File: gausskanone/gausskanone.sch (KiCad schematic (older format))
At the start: 63 parts, among them J3 Power Input, J5 Speedsensor, Q1 Q_NMOS_DGS, Q2 Q_NMOS_DGS, Q3 Q_NMOS_DGS, SW1 SW_DPST, SW2 SW_DPST, U2 Si8220, U3 IE1212D, U5 IL300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

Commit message: Add files via upload
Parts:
- removed U?: LT1037, symbol Amplifier_Operational:OP249
- added R?: 16K, symbol Device:R
- added U? (x2): OPA1678, symbol Amplifier_Operational:OPA1678
- R6: value R -> 2K
- RV?: value R_POT -> 2K
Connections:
- wire segments 272 -> 273
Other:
- note added: "VOUT 6V\n\n"
- note added: "op versorgung +-12V\n"
- note removed: "VOUT\n"
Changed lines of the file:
@@
 P 10900 950
 F 0 "RV?" V 10693 950 50  0000 C CNN
-F 1 "R_POT" V 10784 950 50  0000 C CNN
+F 1 "2K" V 10784 950 50  0000 C CNN
 F 2 "" H 10900 950 50  0001 C CNN
 F 3 "~" H 10900 950 50  0001 C CNN
@@
 $EndComp
 Text Notes 15250 3550 0    50   ~ 0
-VOUT\n
+VOUT 6V\n\n
 Wire Wire Line
 	14400 3600 15300 3600
@@
 $EndComp
 $Comp
-L Amplifier_Operational:OP249 U?
-U 1 1 5DF6E34D
-P 12950 1150
-F 0 "U?" H 12950 1517 50  0000 C CNN
-F 1 "LT1037" H 12950 1426 50  0000 C CNN
-F 2 "" H 12950 1150 50  0001 C CNN
-F 3 "https://www.analog.com/media/en/technical-documentation/data-sheets/OP249.pdf" H 12950 1150 50  0001 C CNN
-	1    12950 1150
-	1    0    0    -1
-$EndComp
-$Comp
 L Connector:Conn_01x02_Female J?
 U 1 1 5E147FCA
@@
 Connection ~ 9400 1050
 Wire Wire Line
-	10100 950  10750 950
-Wire Wire Line
 	10100 1050 10100 950
 Wire Wire Line
@@
 P 11200 1250
 F 0 "R6" H 11270 1296 50  0000 L CNN
-F 1 "R" H 11270 1205 50  0000 L CNN
+F 1 "2K" H 11270 1205 50  0000 L CNN
 F 2 "" V 11130 1250 50  0001 C CNN
 F 3 "~" H 11200 1250 50  0001 C CNN
@@
 	1    0    0    -1
 $EndComp
+$Comp
+L Amplifier_Operational:OPA1678 U?
+U 1 1 5E25FF63
+P 12950 1150
+F 0 "U?" H 12950 1517 50  0000 C CNN
+F 1 "OPA1678" H 12950 1426 50  0000 C CNN
+F 2 "" H 12950 1150 50  0001 C CNN
+F 3 "http://www.ti.com/lit/ds/symlink/opa1678.pdf" H 12950 1150 50  0001 C CNN
+	1    12950 1150
+	1    0    0    -1
+$EndComp
+$Comp
+L Amplifier_Operational:OPA1678 U?
+U 3 1 5E280D7A
+P 15300 1300
+F 0 "U?" H 15258 1346 50  0000 L CNN
+F 1 "OPA1678" H 15258 1255 50  0000 L CNN
+F 2 "" H 15300 1300 50  0001 C CNN
+F 3 "http://www.ti.com/lit/ds/symlink/opa1678.pdf" H 15300 1300 50  0001 C CNN
+	3    15300 1300
+	1    0    0    -1
+$EndComp
+Text Notes 15000 950  0    50   ~ 0
+op versorgung +-12V\n
+$Comp
+L Device:R R?
+U 1 1 5E2B2007
+P 10400 950
+F 0 "R?" H 10470 996 50  0000 L CNN
+F 1 "16K" H 10470 905 50  0000 L CNN
+F 2 "" V 10330 950 50  0001 C CNN
+F 3 "~" H 10400 950 50  0001 C CNN
+	1    10400 950
+	0    1    1    0
+$EndComp
+Wire Wire Line
+	10100 950  10250 950
+Wire Wire Line
+	10550 950  10750 950
 $EndSCHEMATC

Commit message: PCB ready for order
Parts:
- removed C15: CP, symbol Device:CP
- removed Q1, Q2, Q3: Q_NMOS_DGS, symbol Device:Q_NMOS_DGS
- removed R?: 70K, symbol Device:R
- removed SW1, SW2: SW_DPST, symbol Switch:SW_DPST
- removed TP1: UC, symbol Connector:TestPoint
- removed U3: IE1212D, Project:IEXXXXD, symbol Regulator_Switching:CRE1S0305S3C
- removed U?: DA04-11SRWA, Display_7Segment:DA04-11SURKWA, symbol Display_Character:DA04-11SRWA
- added C1, C4: C, Capacitor_SMD:C_0805_2012Metric, symbol Device:C
- added J3: System Bus, Connector_PinHeader_2.54mm:PinHeader_1x02_P2.54mm_Vertical, symbol Connector:Conn_01x02_Female
- added Q1: Overvoltage, Package_TO_SOT_SMD:TO-252-3_TabPin2, symbol Device:Q_NMOS_GDS
- added Q2: CSD19536KTT, Package_TO_SOT_SMD:TO-263-3_TabPin2, symbol Device:Q_NMOS_GDS
- added Q3: DCDC, Package_TO_SOT_SMD:TO-252-3_TabPin2, symbol Device:Q_NMOS_GDS
- added R10: 47K, Resistor_SMD:R_0805_2012Metric, symbol Device:R
- added RV2: 10K, Potentiometer_THT:Potentiometer_Bourns_3339P_Vertical, symbol Device:R_POT
- added RV3: 20K, Potentiometer_THT:Potentiometer_Bourns_3339P_Vertical, symbol Device:R_POT
- added RV4: 2K, Potentiometer_THT:Potentiometer_Bourns_3339P_Vertical, symbol Device:R_POT
- added SW1, SW2: SW_DIP_x01, Button_Switch_THT:SW_PUSH_6mm_H7.3mm, symbol Switch:SW_DIP_x01
- added U2: DPU01, Project:DPU01, symbol Project:DPU01
- C10: renamed from C7; footprint (none) -> Capacitor_SMD:C_0805_2012Metric
- C11: renamed from C8; footprint (none) -> Capacitor_SMD:C_0805_2012Metric
- C12: renamed from C9; footprint (none) -> Capacitor_SMD:C_0805_2012Metric
- C13: renamed from C10; footprint (none) -> Capacitor_SMD:C_0805_2012Metric
- C14: renamed from C11; footprint (none) -> Capacitor_SMD:C_0805_2012Metric
- C15: renamed from C12; footprint (none) -> Capacitor_SMD:C_0805_2012Metric
- C16: renamed from C13; footprint (none) -> Capacitor_SMD:C_0805_2012Metric
- C17: renamed from C14; footprint (none) -> Capacitor_SMD:C_0805_2012Metric
- C2: footprint (none) -> Project:BC 58223
- C3: renamed from C?; footprint (none) -> Capacitor_SMD:C_0805_2012Metric
- C5: renamed from C16; footprint (none) -> Capacitor_SMD:C_0805_2012Metric
- C6: renamed from C4; footprint (none) -> Capacitor_THT:CP_Radial_D6.3mm_P2.50mm
- C8: renamed from C5; footprint (none) -> Capacitor_THT:CP_Radial_D8.0mm_P2.50mm
- C9: renamed from C6; footprint (none) -> Capacitor_SMD:C_0805_2012Metric
- D1: renamed from D2; value 63V -> D Overv; footprint (none) -> Diode_SMD:D_SOD-123
- D2: renamed from D3; value D -> Flyback; footprint (none) -> Diode_SMD:D_SOD-123F
- D3: renamed from D1; value D_Schottky -> D Sec; footprint (none) -> Diode_SMD:D_SOD-123F
- D4: renamed from D9; value D -> D Input; footprint (none) -> Diode_SMD:D_SOD-123F
- D5: renamed from D10; value LED -> Green; footprint (none) -> LED_SMD:LED_0805_2012Metric_Castellated
- D6: renamed from D11; value LED -> Red; footprint (none) -> LED_SMD:LED_0805_2012Metric_Castellated
- D7: value D_Schottky -> D Aux; footprint (none) -> Diode_SMD:D_SOD-123
- D8: footprint (none) -> Diode_SMD:D_SOD-123
- J1: renamed from J3; footprint (none) -> TerminalBlock_RND:TerminalBlock_RND_205-00289_1x04_P5.08mm_Horizontal
- J2: renamed from J5; footprint (none) -> Connector_PinHeader_2.54mm:PinHeader_1x04_P2.54mm_Vertical
- J4: renamed from J?; footprint (none) -> Connector_PinHeader_2.54mm:PinHeader_1x02_P2.54mm_Vertical
- JP1: footprint (none) -> Connector_PinHeader_2.54mm:PinHeader_1x02_P2.54mm_Vertical
- L1: renamed from L2; footprint (none) -> Project:GK-L01
- L2: renamed from L1; footprint (none) -> Project:PA582-AL
- R1: renamed from R?; value 16K -> R; footprint (none) -> Resistor_SMD:R_0805_2012Metric
- R11, R12, R8, R9: footprint (none) -> Resistor_SMD:R_0805_2012Metric
- R13: renamed from R15; footprint (none) -> Resistor_SMD:R_0805_2012Metric
- R14: renamed from R13; footprint (none) -> Resistor_SMD:R_0805_2012Metric
- R15: renamed from R14; value Curr Sense -> 82m; footprint (none) -> Resistor_SMD:R_1812_4532Metric
- R16: renamed from R20; footprint (none) -> Resistor_SMD:R_0805_2012Metric
- R17: renamed from R16; footprint (none) -> Resistor_SMD:R_0805_2012Metric
- R18: renamed from R17; footprint (none) -> Resistor_SMD:R_0805_2012Metric
- R19: renamed from R18; footprint (none) -> Resistor_SMD:R_0805_2012Metric
- R2, R6: renamed from R?; footprint (none) -> Resistor_SMD:R_0805_2012Metric
- R20: renamed from R19; footprint (none) -> Resistor_SMD:R_0805_2012Metric
- R3: renamed from R2; value R -> 10K; footprint (none) -> Resistor_SMD:R_1812_4532Metric
- R4: value R -> 330R; footprint (none) -> Resistor_SMD:R_1812_4532Metric
- R5: renamed from R6; value 2K -> R; footprint (none) -> Resistor_SMD:R_0805_2012Metric
- R7: renamed from R3; footprint (none) -> Resistor_SMD:R_0805_2012Metric
- RV1: renamed from RV?; footprint (none) -> Potentiometer_THT:Potentiometer_Bourns_3339P_Vertical
- TP2: footprint (none) -> TestPoint:TestPoint_Loop_D1.80mm_Drill1.0mm_Beaded
- U1: renamed from U?; footprint (none) -> Package_SO:SOIC-8_3.9x4.9mm_P1.27mm; symbol Amplifier_Operational:OPA1678 -> gausskanone-rescue:OPA1678-Amplifier_Operational
- U3: renamed from U5; footprint (none) -> Package_DIP:PowerIntegrations_SMD-8
- renumbered U2 to U4, U7 to U5
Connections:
- net labels added: ISO-12V, UMeas
- net labels removed: ISO12V
- wire segments 273 -> 275
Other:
- note removed: "VOUT 6V\n\n"
- moved on the sheet: C5, C6, J4, R1, R5, R6, R7, RV1

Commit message: Dimensionierungen
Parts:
- C1, C10, C4, C5, C9: value C -> 100P
- C11: value C -> 220N
- C14, C16, C17: value C -> NC
- C15: value C -> 2N2
- D8: value 10V -> 10V NC
- R1: value R -> 8K2
- R11: value R -> 400K
- R12, R14, R19, R20, R8: value R -> 0R
- R17: value R -> 22K
- R18: value R -> 10K
- R2: value 100 -> 100R
- R5: value R -> 91K
- R9: value R -> 300R
- RV1: value 2K -> 10K
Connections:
- net +12V: now also C9.2; no longer C9.1
- net GND: now also C9.1; no longer C9.2
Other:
- moved on the sheet: C9
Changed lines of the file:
@@
 P 11200 1400
 F 0 "RV1" V 10993 1400 50  0000 C CNN
-F 1 "2K" V 11084 1400 50  0000 C CNN
+F 1 "10K" V 11084 1400 50  0000 C CNN
 F 2 "Potentiometer_THT:Potentiometer_Bourns_3339P_Vertical" H 11200 1400 50  0001 C CNN
 F 3 "~" H 11200 1400 50  0001 C CNN
@@
 P 14050 1150
 F 0 "R2" V 13843 1150 50  0000 C CNN
-F 1 "100" V 13934 1150 50  0000 C CNN
+F 1 "100R" V 13934 1150 50  0000 C CNN
 F 2 "Resistor_SMD:R_0805_2012Metric" V 13980 1150 50  0001 C CNN
 F 3 "~" H 14050 1150 50  0001 C CNN
@@
 P 10150 1950
 F 0 "C5" H 10265 1996 50  0000 L CNN
-F 1 "C" H 10265 1905 50  0000 L CNN
+F 1 "100P" H 10265 1905 50  0000 L CNN
 F 2 "Capacitor_SMD:C_0805_2012Metric" H 10188 1800 50  0001 C CNN
 F 3 "~" H 10150 1950 50  0001 C CNN
@@
 P 11200 1800
 F 0 "R5" H 11270 1846 50  0000 L CNN
-F 1 "R" H 11270 1755 50  0000 L CNN
+F 1 "91K" H 11270 1755 50  0000 L CNN
 F 2 "Resistor_SMD:R_0805_2012Metric" V 11130 1800 50  0001 C CNN
 F 3 "~" H 11200 1800 50  0001 C CNN
@@
 P 9300 2300
 F 0 "R8" V 9093 2300 50  0000 C CNN
-F 1 "R" V 9184 2300 50  0000 C CNN
+F 1 "0R" V 9184 2300 50  0000 C CNN
 F 2 "Resistor_SMD:R_0805_2012Metric" V 9230 2300 50  0001 C CNN
 F 3 "~" H 9300 2300 50  0001 C CNN
@@
 P 10050 3650
 F 0 "R9" H 9900 3700 50  0000 L CNN
-F 1 "R" H 9900 3600 50  0000 L CNN
+F 1 "300R" H 9800 3600 50  0000 L CNN
 F 2 "Resistor_SMD:R_0805_2012Metric" V 9980 3650 50  0001 C CNN
 F 3 "~" H 10050 3650 50  0001 C CNN
@@
 P 1400 8300
 F 0 "R17" H 1330 8254 50  0000 R CNN
-F 1 "R" H 1330 8345 50  0000 R CNN
+F 1 "22K" H 1330 8345 50  0000 R CNN
 F 2 "Resistor_SMD:R_0805_2012Metric" V 1330 8300 50  0001 C CNN
 F 3 "~" H 1400 8300 50  0001 C CNN
@@
 P 1400 7900
 F 0 "C15" H 1515 7946 50  0000 L CNN
-F 1 "C" H 1515 7855 50  0000 L CNN
+F 1 "2N2" H 1515 7855 50  0000 L CNN
 F 2 "Capacitor_SMD:C_0805_2012Metric" H 1438 7750 50  0001 C CNN
 F 3 "~" H 1400 7900 50  0001 C CNN
@@
 P 1750 7900
 F 0 "C16" H 1865 7946 50  0000 L CNN
-F 1 "C" H 1865 7855 50  0000 L CNN
+F 1 "NC" H 1865 7855 50  0000 L CNN
 F 2 "Capacitor_SMD:C_0805_2012Metric" H 1788 7750 50  0001 C CNN
 F 3 "~" H 1750 7900 50  0001 C CNN
@@
 P 2850 8800
 F 0 "R20" H 2780 8754 50  0000 R CNN
-F 1 "R" H 2780 8845 50  0000 R CNN
+F 1 "0R" H 2780 8845 50  0000 R CNN
 F 2 "Resistor_SMD:R_0805_2012Metric" V 2780 8800 50  0001 C CNN
 F 3 "~" H 2850 8800 50  0001 C CNN
@@
 P 3100 8550
 F 0 "R18" V 2893 8550 50  0000 C CNN
-F 1 "R" V 2984 8550 50  0000 C CNN
+F 1 "10K" V 2984 8550 50  0000 C CNN
 F 2 "Resistor_SMD:R_0805_2012Metric" V 3030 8550 50  0001 C CNN
 F 3 "~" H 3100 8550 50  0001 C CNN
@@
 P 3800 8800
 F 0 "D8" V 3754 8879 50  0000 L CNN
-F 1 "10V" V 3845 8879 50  0000 L CNN
+F 1 "10V NC" V 3845 8879 50  0000 L CNN
 F 2 "Diode_SMD:D_SOD-123" H 3800 8800 50  0001 C CNN
 F 3 "~" H 3800 8800 50  0001 C CNN
@@
 P 4600 8800
 F 0 "C17" H 4715 8846 50  0000 L CNN
-F 1 "C" H 4715 8755 50  0000 L CNN
+F 1 "NC" H 4715 8755 50  0000 L CNN
 F 2 "Capacitor_SMD:C_0805_2012Metric" H 4638 8650 50  0001 C CNN
 F 3 "~" H 4600 8800 50  0001 C CNN
@@
 P 4850 8550
 F 0 "R19" V 4643 8550 50  0000 C CNN
-F 1 "R" V 4734 8550 50  0000 C CNN
+F 1 "0R" V 4734 8550 50  0000 C CNN
 F 2 "Resistor_SMD:R_0805_2012Metric" V 4780 8550 50  0001 C CNN
 F 3 "~" H 4850 8550 50  0001 C CNN
@@
 P 1450 5700
 F 0 "R11" H 1520 5746 50  0000 L CNN
-F 1 "R" H 1520 5655 50  0000 L CNN
+F 1 "400K" H 1520 5655 50  0000 L CNN
 F 2 "Resistor_SMD:R_0805_2012Metric" V 1380 5700 50  0001 C CNN
 F 3 "~" H 1450 5700 50  0001 C CNN
@@
 P 1450 6200
 F 0 "C10" H 1565 6246 50  0000 L CNN
-F 1 "C" H 1565 6155 50  0000 L CNN
+F 1 "100P" H 1565 6155 50  0000 L CNN
 F 2 "Capacitor_SMD:C_0805_2012Metric" H 1488 6050 50  0001 C CNN
 F 3 "~" H 1450 6200 50  0001 C CNN
@@
 P 1800 6950
 F 0 "C11" H 1915 6996 50  0000 L CNN
-F 1 "C" H 1915 6905 50  0000 L CNN
+F 1 "220N" H 1915 6905 50  0000 L CNN
 F 2 "Capacitor_SMD:C_0805_2012Metric" H 1838 6800 50  0001 C CNN
 F 3 "~" H 1800 6950 50  0001 C CNN
@@
 P 5050 6150
 F 0 "R12" V 4843 6150 50  0000 C CNN
-F 1 "R" V 4934 6150 50  0000 C CNN
+F 1 "0R" V 4934 6150 50  0000 C CNN
 F 2 "Resistor_SMD:R_0805_2012Metric" V 4980 6150 50  0001 C CNN
 F 3 "~" H 5050 6150 50  0001 C CNN
@@
 	0    1    1    0
 $EndComp
-Wire Wire Line
-	3150 4900 3150 5050
-Connection ~ 3150 4900
-Wire Wire Line
-	3500 4900 3150 4900
-Wire Wire Line
-	3500 4750 3500 4900
-Wire Wire Line
-	3500 4350 4150 4350
-Connection ~ 3500 4350
-Wire Wire Line
-	3500 4350 3500 4450
 $Comp
 L Device:C C9
 U 1 1 5DF59379
-P 3500 4600
-F 0 "C9" H 3615 4646 50  0000 L CNN
-F 1 "C" H 3615 4555 50  0000 L CNN
-F 2 "Capacitor_SMD:C_0805_2012Metric" H 3538 4450 50  0001 C CNN
-F 3 "~" H 3500 4600 50  0001 C CNN
-	1    3500 4600
-	1    0    0    -1
-$EndComp
-Wire Wire Line
-	3150 4750 3150 4900
+P 11000 3500
+F 0 "C9" H 11115 3546 50  0000 L CNN
+F 1 "100P" H 11115 3455 50  0000 L CNN
+F 2 "Capacitor_SMD:C_0805_2012Metric" H 11038 3350 50  0001 C CNN
+F 3 "~" H 11000 3500 50  0001 C CNN
+	1    11000 3500
+	0    1    1    0
+$EndComp
 $Comp
 L power:GND #PWR07
@@
 Wire Wire Line
 	3150 3900 3150 4200
-Wire Wire Line
-	3150 4350 3500 4350
 $Comp
 L power:+12V #PWR02
@@
 P 5150 6450
 F 0 "R14" V 4943 6450 50  0000 C CNN
-F 1 "R" V 5034 6450 50  0000 C CNN
+F 1 "0R" V 5034 6450 50  0000 C CNN
 F 2 "Resistor_SMD:R_0805_2012Metric" V 5080 6450 50  0001 C CNN
 F 3 "~" H 5150 6450 50  0001 C CNN
@@
 P 4650 6950
 F 0 "C14" H 4765 6996 50  0000 L CNN
-F 1 "C" H 4765 6905 50  0000 L CNN
+F 1 "NC" H 4765 6905 50  0000 L CNN
 F 2 "Capacitor_SMD:C_0805_2012Metric" H 4688 6800 50  0001 C CNN
 F 3 "~" H 4650 6950 50  0001 C CNN
@@
 P 11200 1000
 F 0 "R1" H 11270 1046 50  0000 L CNN
-F 1 "R" H 11270 955 50  0000 L CNN
+F 1 "8K2" H 11270 955 50  0000 L CNN
 F 2 "Resistor_SMD:R_0805_2012Metric" V 11130 1000 50  0001 C CNN
 F 3 "~" H 11200 1000 50  0001 C CNN
@@
 P 11900 1900
 F 0 "C4" V 11648 1900 50  0000 C CNN
-F 1 "C" V 11739 1900 50  0000 C CNN
+F 1 "100P" V 11739 1900 50  0000 C CNN
 F 2 "Capacitor_SMD:C_0805_2012Metric" H 11938 1750 50  0001 C CNN
 F 3 "~" H 11900 1900 50  0001 C CNN
@@
 P 11900 1300
 F 0 "C1" V 11648 1300 50  0000 C CNN
-F 1 "C" V 11739 1300 50  0000 C CNN
+F 1 "100P" V 11739 1300 50  0000 C CNN
 F 2 "Capacitor_SMD:C_0805_2012Metric" H 11938 1150 50  0001 C CNN
 F 3 "~" H 11900 1300 50  0001 C CNN
@@
 	9550 6750 10550 6750
 Wire Wire Line
-	11200 3350 11200 4400
-Wire Wire Line
-	10800 3350 10800 4300
+	11200 3350 11200 3500
+Wire Wire Line
+	10800 3350 10800 3500
 Wire Wire Line
 	14400 3150 14400 3450
@@
 Wire Wire Line
 	14400 4200 14400 4400
+Wire Wire Line
+	10850 3500 10800 3500
+Connection ~ 10800 3500
+Wire Wire Line
+	10800 3500 10800 4300
+Wire Wire Line
+	11150 3500 11200 3500
+Connection ~ 11200 3500
+Wire Wire Line
+	11200 3500 11200 4400
+Wire Wire Line
+	3150 4750 3150 5050
+Wire Wire Line
+	3150 4350 4150 4350
 $EndSCHEMATC

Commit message: powerpoint
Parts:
- U2: symbol Project:DPU01 -> gausskanone-rescue:DPU01-Project
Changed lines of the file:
@@
 EESchema Schematic File Version 4
 LIBS:gausskanone-cache
-EELAYER 26 0
+EELAYER 30 0
 EELAYER END
 $Descr A3 16535 11693
@@
 Connection ~ 7400 1900
 $Comp
-L Project:DPU01 U2
+L gausskanone-rescue:DPU01-Project U2
 U 1 1 5E021FEC
 P 10500 2700

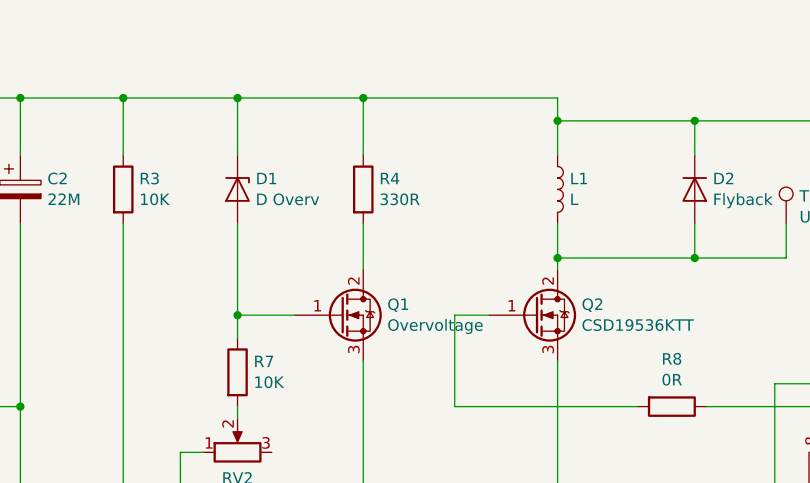
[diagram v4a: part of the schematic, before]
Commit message: ueberspannung
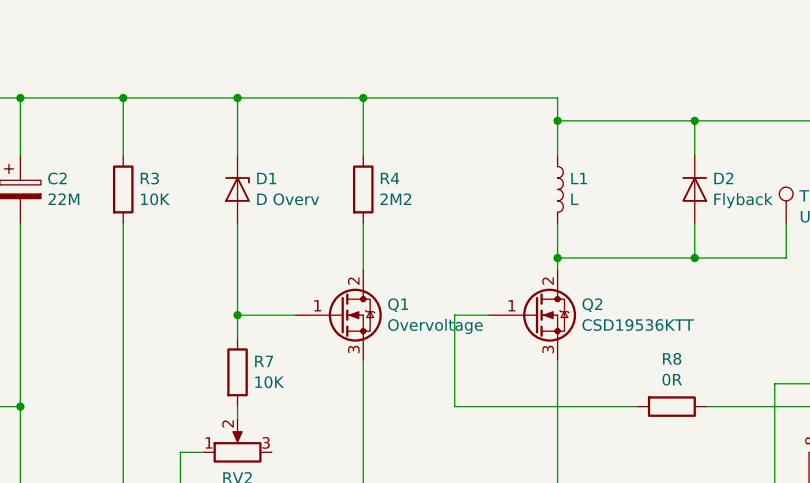
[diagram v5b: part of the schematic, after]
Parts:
- R4: value 330R -> 2M2
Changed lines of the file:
@@
 P 7950 1350
 F 0 "R4" H 8020 1396 50  0000 L CNN
-F 1 "330R" H 8020 1305 50  0000 L CNN
+F 1 "2M2" H 8020 1305 50  0000 L CNN
 F 2 "Resistor_SMD:R_1812_4532Metric" V 7880 1350 50  0001 C CNN
 F 3 "~" H 7950 1350 50  0001 C CNN
